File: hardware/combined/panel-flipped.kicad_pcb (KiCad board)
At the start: 2 copper layers, 62 x 104.3 mm, 5 parts

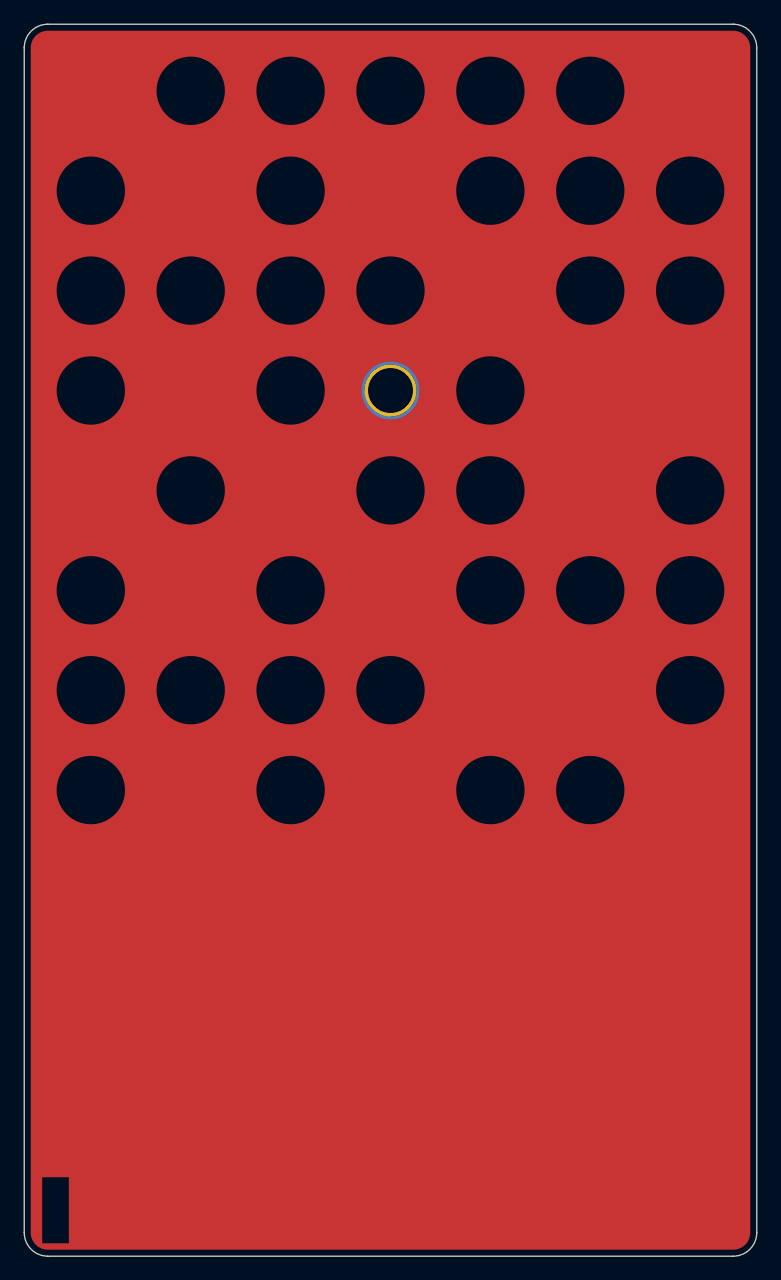
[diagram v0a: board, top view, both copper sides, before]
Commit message: Fab package: regenerated from the routed rev 2026.11 board (W-1091)
138 placements on AirWriter, 61 on Lite; drill floor 0.30 mm. The combined
panel's DRC under its default rules shows only the known kinds; R17 and D3 add
one copper-edge and one silk-edge item each way, both clear under the main
board's own 0.25 mm edge rule.
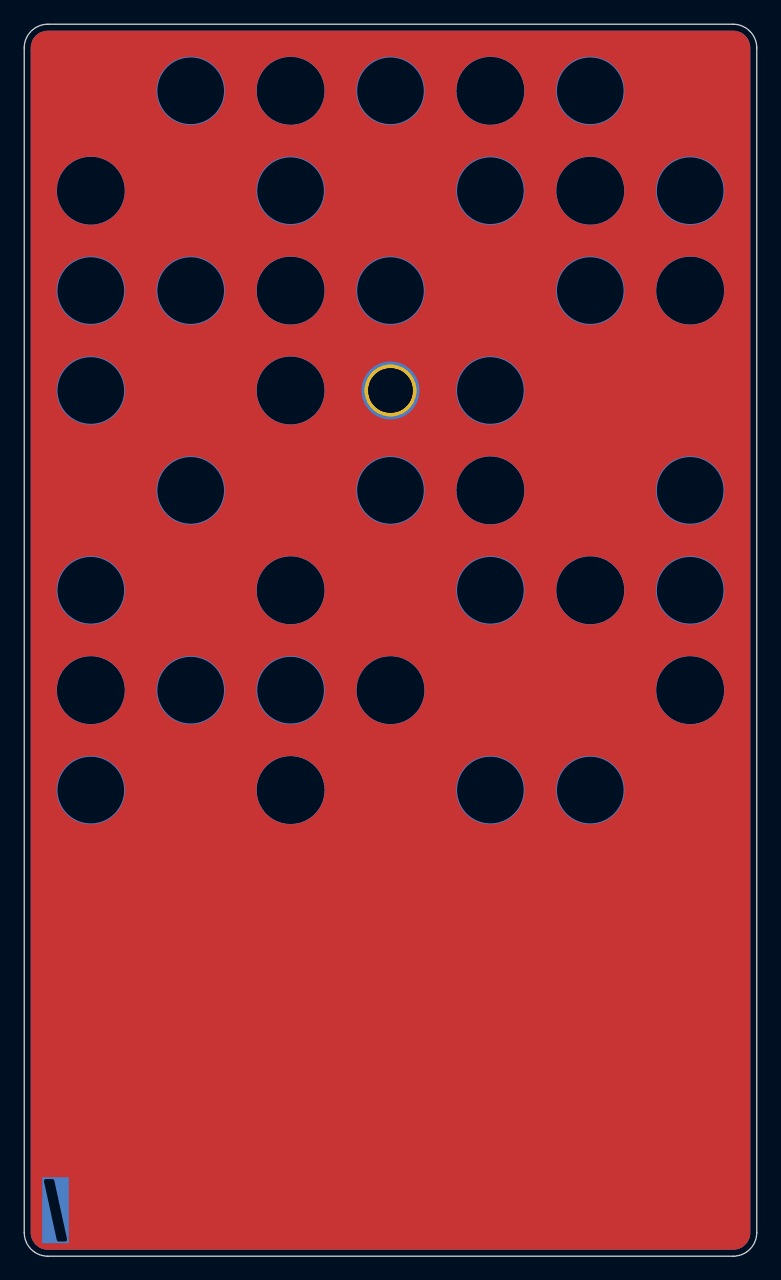
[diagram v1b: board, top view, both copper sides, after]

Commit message: Panel: Frame 16 art, rev 2026.11 (W-1091)
Wells's Frame 16 export, with only its dot area left out: the dots are the
committed ones, pixel for pixel. The rest is Frame 16's: "rev 2026.11", the
text block a few pixels left and up, the port labels on one baseline, and a
power slash of about 1.0 x 5.75 mm (was 0.8 x 5.2), centred 0.3 mm further up.
D3 stays where it is: it can't go west of J1's courtyard, and its 3 mm face
still covers the slash's width. The lattice's D3 tube is re-cut round the new
window (131 tests pass); the combined panel and fab package are rebuilt.

Refs: W-1091
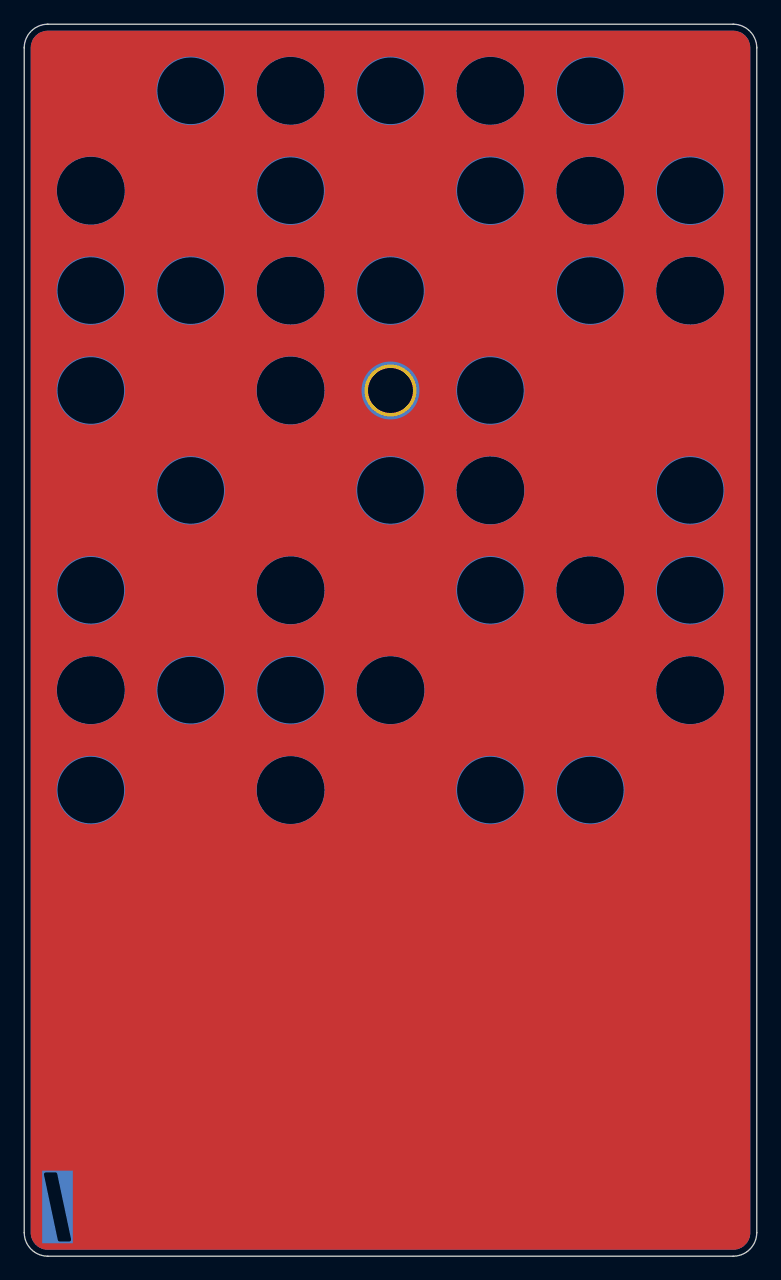
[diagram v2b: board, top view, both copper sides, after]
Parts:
- moved MT2 86.3 mm to (5.64, 5.64)
- moved MT3 86.3 mm to (56.4, 91.9)
- moved MT1 50.7 mm to (56.4, 5.64)
- moved MT4 47.7 mm to (8.64, 91.9)
- renumbered MT2 to MT1, MT4 to MT2, MT1 to MT3, MT3 to MT4
